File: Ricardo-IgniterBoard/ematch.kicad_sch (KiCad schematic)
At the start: 32 parts, among them J501 Conn_01x02_Male, J502 Conn_01x02_Male, J503 Conn_01x02_Male, Q501 BSZ025N04LS, Q502 BSZ025N04LS, Q503 BSZ025N04LS, U501 LTV-247, U502 LTV-247

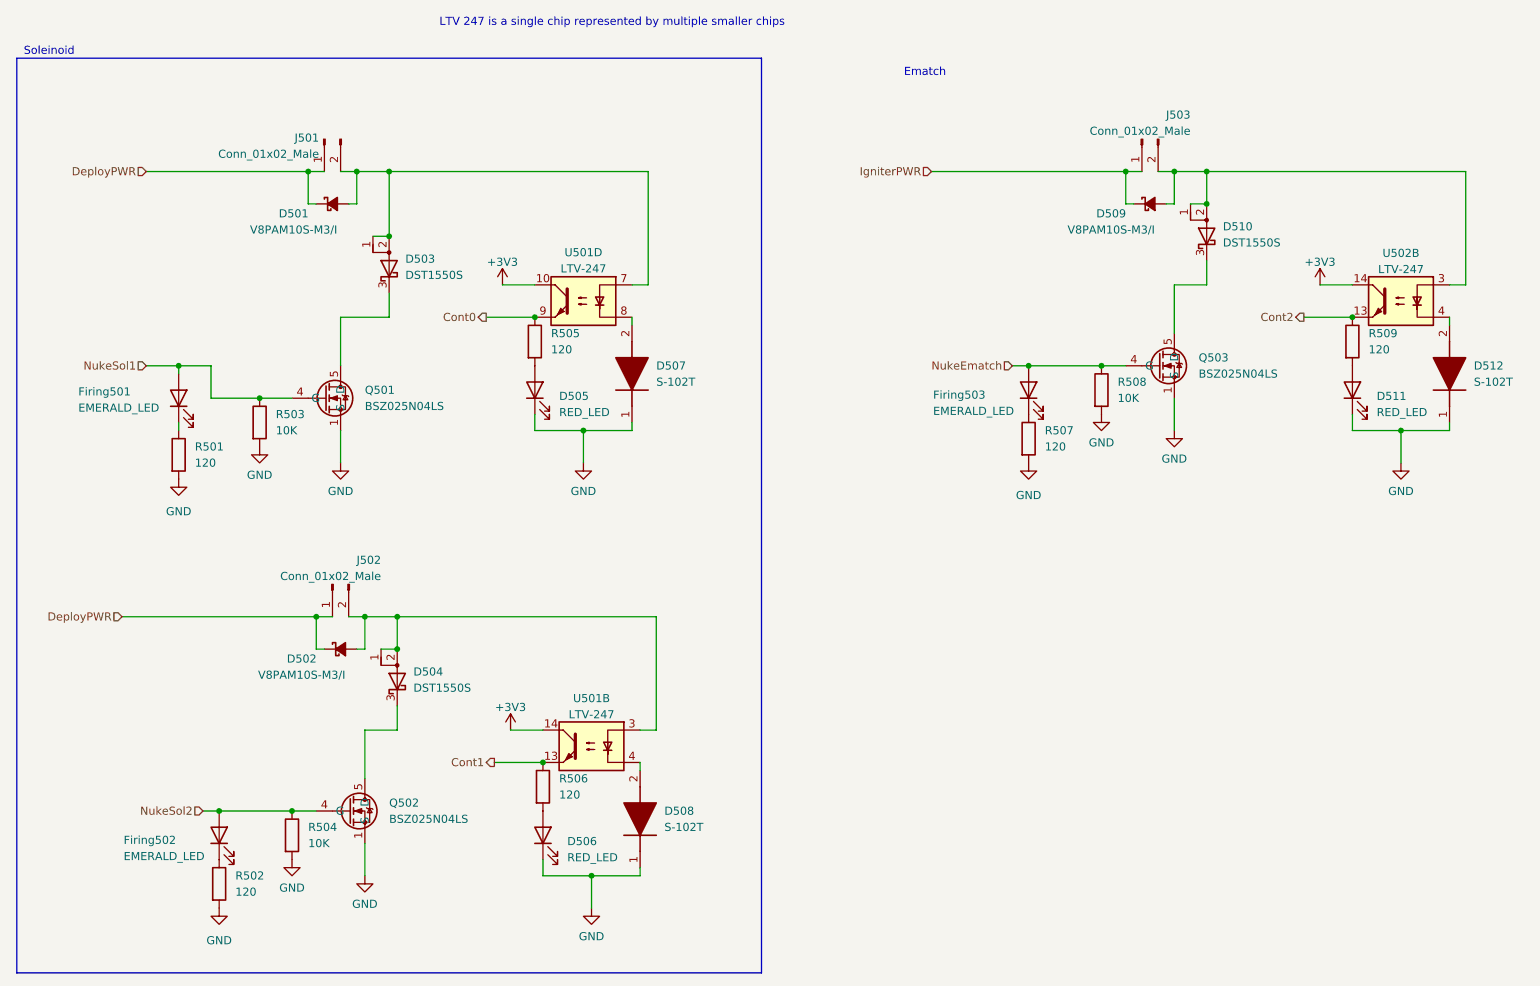
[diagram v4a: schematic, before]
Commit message: some more changes
added current sensor for solenoid, fixed optocouplers
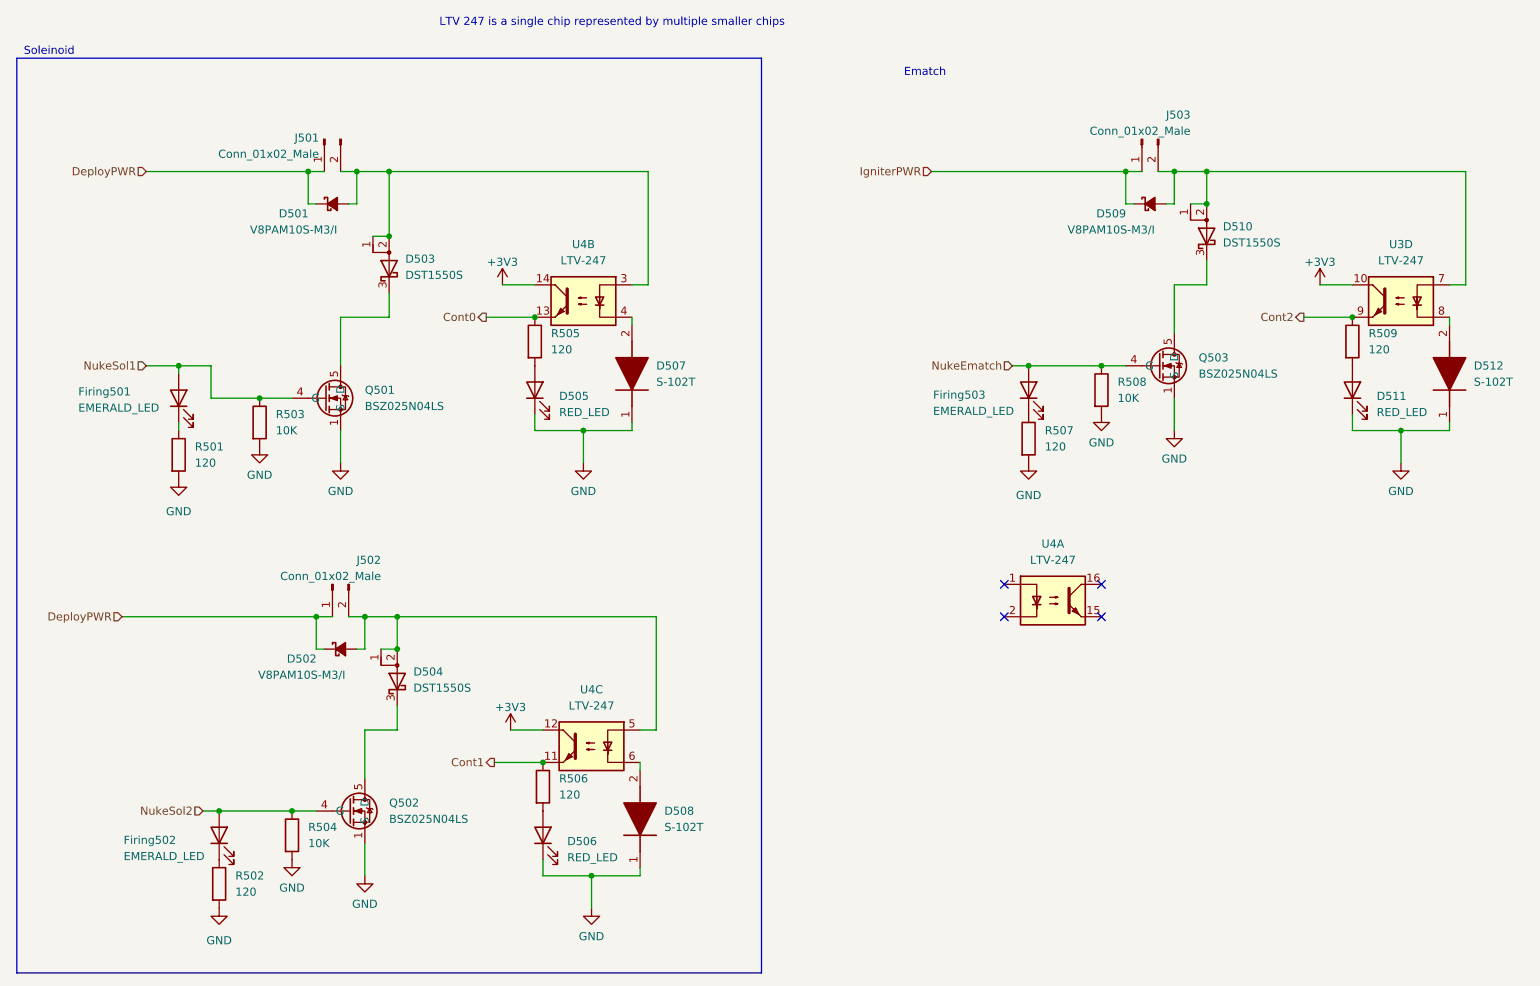
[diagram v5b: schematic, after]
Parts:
- removed U501, U502: LTV-247, Package_SO:SOP-16_4.4x10.4mm_P1.27mm, symbol Isolator:LTV-247
- added U3, U4: LTV-247, Package_SO:SOP-16_4.4x10.4mm_P1.27mm, symbol Isolator:LTV-247
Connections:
- net +3V3: now also U3.10, U4.12, U4.14
- net Cont0: now also U4.13
- net Cont1: now also U4.11
- net Cont2: now also U3.9
- net at D501.2 (A), D503.1 (A), D503.2 (A)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: now also U4.3
- net at D508.2 (A): now also U4.6
- net at D509.2 (A), D510.1 (A), D510.2 (A)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: now also U3.7
- net at D502.2 (A), D504.1 (A), D504.2 (A)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: now also U4.5
- net at D512.2 (A): now also U3.8
- net at D507.2 (A): now also U4.4
- no-connect marks 0 -> 4
